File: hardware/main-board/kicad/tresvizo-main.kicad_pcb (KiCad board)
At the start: 4 copper layers, 50 x 76 mm, 143 parts, among them J101 PANEL_USB, J102 BATTERY, J301 U.FL, J302 UM980_AUX, J401 TF-015, J402 PANEL_UI, J403 OLED, J404 NTC, Q101 AO3400A, Q102 AO3401A, Q103 AO3400A, Q401 AO3401A, Q402 AO3400A, SW201 RESET, SW202 BOOT, U101 USBLC6-2SC6, U102 BQ25798RQMR, U103 MAX17048G+T10, U105 TPS62903RPJR, U106 TPS22919DCKR, U201 ESP32-S3-MINI-1-N4R2, U301 UM980, U302 TPS22945DCKR, U401 BMI088

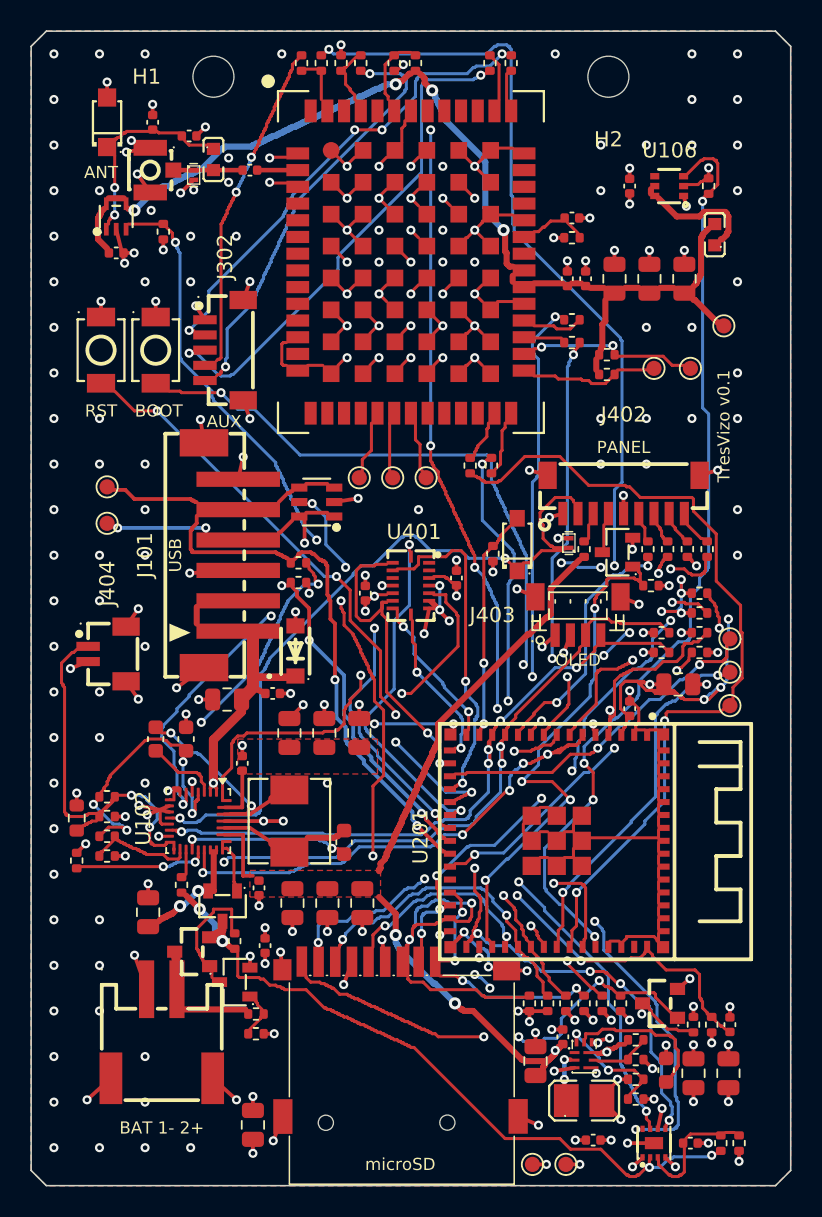
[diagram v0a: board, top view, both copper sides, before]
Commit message: Placa principal v0.2: UM980 y BMI088 por cable, conectores hacia cantos o zonas libres, placa panel-usb y un solo panel para JLCPCB
- 46 x 64 mm, 4 capas. El UM980 queda en su carrier BDLX por J301 (GH 8) con 5 V conmutable
  (TPS63070, GPIO45) y el BMI088 vuelve a la tapa por I2C en un segundo bus (J405, GH 7).
- Todos los conectores de cable son GH o SH de 8 pines o menos (kit del propietario), salvo la
  batería (PH 2). Cada uno apunta a un canto o a una zona libre con sitio para la clavija
  enchufada y su cable: áreas de regla clavija_* en el DRC y kicad/plugs.json para el CAD.
- La placa sube 2.5 mm en el tubo (z 23.5-87.5) para que las clavijas del canto inferior tengan
  7.6 mm hasta la base; rieles propuestos en z 39-90 y agujeros nuevos. Comprobada en FreeCAD
  contra V2.2 con modelos 3D y clavijas: sin choques.
- Cargador según el ejemplo de TI: bootstrap junto a sus pines (0.9 y 1.6 mm), salida en abanico
  de la fila inferior y potencia solo por capas externas.
- Placa panel-usb (USB-C a ras de la tapa del panel, GH 8 a J101) y panel de las dos placas con un
  BOM y un CPL (panelize.py, 82.8 x 78 mm).
- Serigrafía sin solapes (silk_clean.py) y logotipo de TresVizo con www.tresvizo.com.
- ERC 0; DRC con 0 errores, 0 avisos, 0 sin conectar y 0 diferencias de paridad en las dos
  placas y el panel. Costo estimado de montaje y piezas: 211 USD por 5 juegos en un panel, sin
  el PCB desnudo.
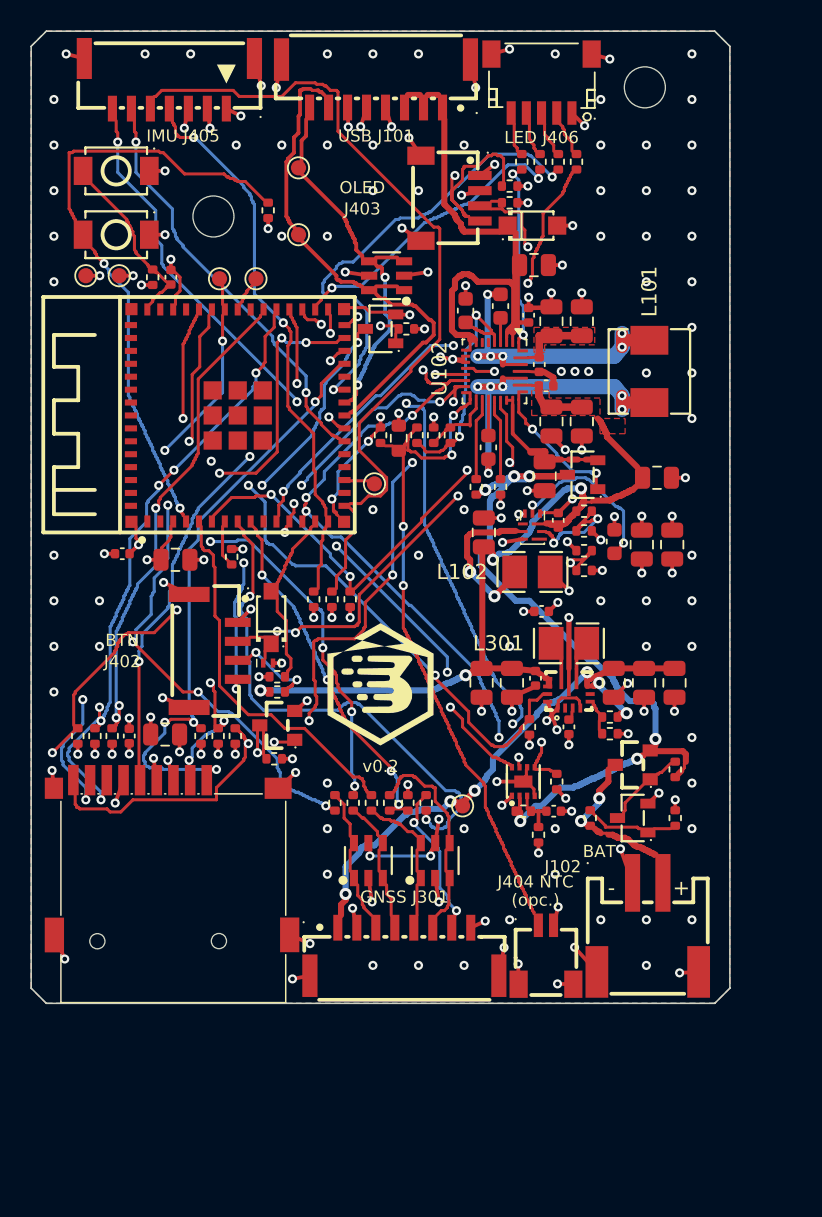
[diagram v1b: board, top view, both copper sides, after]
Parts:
- removed C121, C308, C403, C404: 100nF, Capacitor_SMD:C_0402_1005Metric
- removed C122: 1uF, Capacitor_SMD:C_0402_1005Metric
- removed C309, C310: 100pF, Capacitor_SMD:C_0402_1005Metric
- removed D301: SMF5.0A, tresvizo_lcsc:SOD-123FL_L2.7-W1.8-LS3.8-RD
- removed D302: PESD5V0F1BL, tresvizo_lcsc:SOD-882_L1.0-W0.6-BI
- removed FB101: BLM18PG121SN1D, tresvizo_lcsc:L0603
- removed J302: UM980_AUX, tresvizo_lcsc:CONN-SMD_5P-P1.00_BM05B-SRSS-TB
- removed R120, R122: 100k, Resistor_SMD:R_0402_1005Metric
- removed R121: 22k, Resistor_SMD:R_0402_1005Metric
- removed R310, R311, R313: 100, Resistor_SMD:R_0402_1005Metric
- removed R312: 10k, Resistor_SMD:R_0402_1005Metric
- removed R314, R315, R316: 1k, Resistor_SMD:R_0402_1005Metric
- removed TP302: BIF2, TestPoint:TestPoint_Pad_D1.0mm
- removed TP303: PVT, TestPoint:TestPoint_Pad_D1.0mm
- removed TP304: RTK, TestPoint:TestPoint_Pad_D1.0mm
- removed TP305: ERR, TestPoint:TestPoint_Pad_D1.0mm
- removed TP306: 3V3_GNSS, TestPoint:TestPoint_Pad_D1.0mm
- removed U106: TPS22919DCKR, tresvizo_lcsc:SC-70-6_L2.2-W1.3-P0.65-LS2.1-BR
- removed U401: BMI088, tresvizo_lcsc:LGA-16_L4.5-W3.0-P0.50-BL
- added J405: IMU, tresvizo_lcsc:CONN-SMD_SM7B-GHS-TB-LF-SN, F.Cu at (109.1, 103.5)
- added J406: LEDS, tresvizo_lcsc:CONN-SMD_SM05B-SRSS-TB-LF-SN, F.Cu at (133.6, 103.5)
- added R414: 4.7k, Resistor_SMD:R_0402_1005Metric, F.Cu at (118.6, 137.4)
- added R415: 4.7k, Resistor_SMD:R_0402_1005Metric, F.Cu at (119.8, 137.4)
- added U303: USBLC6-2SC6, tresvizo_lcsc:SOT-23-6_L2.9-W1.6-P0.95-LS2.8-BL, F.Cu at (126.6, 154.6)
- C106, C107: value 10uF -> 22uF
- C108, C112, C116, C303: value 10uF -> 100nF; footprint Capacitor_SMD:C_0805_2012Metric -> Capacitor_SMD:C_0402_1005Metric
- C109, C113: value 100nF -> 22uF; footprint Capacitor_SMD:C_0402_1005Metric -> Capacitor_SMD:C_0805_2012Metric
- C111, C301, C302: value 22uF -> 10uF
- C114, C120: value 22uF -> 100nF; footprint Capacitor_SMD:C_0805_2012Metric -> Capacitor_SMD:C_0402_1005Metric
- C115: value 100nF -> 10uF; footprint Capacitor_SMD:C_0402_1005Metric -> Capacitor_SMD:C_0805_2012Metric
- C117: value 100nF -> 47nF; footprint Capacitor_SMD:C_0402_1005Metric -> Capacitor_SMD:C_0603_1608Metric
- C118: value 47nF -> 22uF; footprint Capacitor_SMD:C_0603_1608Metric -> Capacitor_SMD:C_0805_2012Metric
- C305: value 100pF -> 22uF; footprint Capacitor_SMD:C_0402_1005Metric -> Capacitor_SMD:C_0805_2012Metric
- C306, C307: value 1uF -> 22uF; footprint Capacitor_SMD:C_0402_1005Metric -> Capacitor_SMD:C_0805_2012Metric
- D101: value SMF20A -> SMF15A; footprint tresvizo_lcsc:SOD-123F_L2.8-W1.8-LS3.7-RD -> tresvizo_lcsc:SOD-123FL_L2.7-W1.8-LS3.8-RD
- J101: footprint tresvizo_lcsc:CONN-SMD_6P-P2.00_B6B-PH-SM4-TB-LF-SN -> tresvizo_lcsc:CONN-SMD_8P-P1.25_XUNPU-WAFER-GH1.25-8PWB
- J301: value U.FL -> GNSS; footprint tresvizo_lcsc:IPEX-SMD_BWIPX-1-001E -> tresvizo_lcsc:CONN-SMD_8P-P1.25_XUNPU-WAFER-GH1.25-8PWB
- J402: value PANEL_UI -> BOTON; footprint tresvizo_lcsc:CONN-SMD_9P-P1.00_BM09B-SRSS-TB -> tresvizo_lcsc:CONN-SMD_4P-P1.25_SM04B-GHS-TB-LF-SN
- J403: footprint tresvizo_lcsc:CONN-SMD_BM04B-SRSS-TB -> tresvizo_lcsc:CONN-SMD_4P-P1.00_SM04B-SRSS-TB-LF-SN
- J404: footprint tresvizo_lcsc:CONN-TH_BM02B-SRSS-TB-LF-SN -> tresvizo_lcsc:CONN-SMD_2P-P1.00_SM02B-SRSS-TB-LF-SN
- L301: value 68nH -> 1uH; footprint tresvizo_lcsc:L0603 -> tresvizo_lcsc:L2520
- R101, R117: value 0 -> 10k
- R102: value 0 -> 22k
- R103: value 10k -> 4.7k
- R104: value 22k -> 5.1k
- R105: value 4.7k -> 30k; footprint Resistor_SMD:R_0402_1005Metric -> Resistor_SMD:R_0603_1608Metric
- R106: value 5.1k -> 10k
- R107: value 30k -> 100; footprint Resistor_SMD:R_0603_1608Metric -> Resistor_SMD:R_0402_1005Metric
- R109, R307, R309: value 100 -> 1k
- R110: value 10k -> 1M
- R111, R308: value 1k -> 100k
- R113: value 100k -> 0
- R114: value 1M -> 10k
- R116, R119: value 10k -> 22k
- R118: value 22k -> 100k
- R301: value 0 -> 100k
- R302: value 10k -> 5.1k
- R303, R304: value 10k -> 1k
- R305: value 100k -> 100
- R306: value 1k -> 100
- TP301: value BIF1 -> 5V_GNSS
- U301: value UM980 -> TPS63070RNMR; footprint tresvizo:UM980 -> tresvizo_lcsc:VQFN-15_L3.0-W2.5-P0.50-BL
- U302: value TPS22945DCKR -> USBLC6-2SC6; footprint tresvizo_lcsc:SC-70-5_L2.1-W1.3-P0.65-LS2.1-BL -> tresvizo_lcsc:SOT-23-6_L2.9-W1.6-P0.95-LS2.8-BL
- moved TP201 65.5 mm to (103.6, 116.1)
- moved TP202 65.5 mm to (105.8, 116.1)
- moved R201 61.4 mm to (108.0, 116.2)
- moved C203 61.4 mm to (109.2, 116.2)
- moved J301 53.9 mm to (124.6, 160.6), turned to 0 degrees
- moved R109 52.6 mm to (132.3, 108.6)
- moved R305 48.7 mm to (121.2, 150.8)
- moved C307 46.4 mm to (142.3, 142.9), turned to -90 degrees
- moved U302 45.5 mm to (122.2, 154.6)
- moved R302 44.9 mm to (138.1, 145.2), turned to 180 degrees
- moved TP205 43.8 mm to (112.4, 116.3)
- moved C115 42.4 mm to (129.8, 133.0), turned to 90 degrees
- moved R117 41.6 mm to (136.4, 132.9), turned to 0 degrees
- moved TP204 40.5 mm to (114.8, 116.3)
- moved R202 39.7 mm to (115.6, 111.8), turned to 90 degrees
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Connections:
- net /microSD, IMU y panel/BTN_LED_A renamed /microSD, IMU por conector y panel/BTN_LED_A
- net /microSD, IMU y panel/BTN_LED_K renamed /microSD, IMU por conector y panel/BTN_LED_K
- net /microSD, IMU y panel/SD_CD_N renamed /microSD, IMU por conector y panel/SD_CD_N
- C109 pad 1: /Alimentación, carga y batería/PMID -> VSYS
- C113 pad 1: VSYS -> /Alimentación, carga y batería/VBAT_CHG
- C114 pad 1: /Alimentación, carga y batería/VBAT_CHG -> /Alimentación, carga y batería/FG_VDD
- C115 pad 1: /Alimentación, carga y batería/FG_VDD -> VSYS
- C117 pad 1: VSYS -> /Alimentación, carga y batería/BUCK_SS
- C118 pad 1: /Alimentación, carga y batería/BUCK_SS -> +3V3
- C301 pad 1: +3V3_GNSS -> VSYS
- C302 pad 1: +3V3_GNSS -> VSYS
- C303 pad 1: +3V3_GNSS -> VSYS
- C304 pad 1: +3V3_GNSS -> /GNSS: carrier UM980 por conector y su 5 V/GNSS_VAUX
- C305 pad 1: +3V3_GNSS -> /GNSS: carrier UM980 por conector y su 5 V/GNSS_5V
- C306 pad 1: /GNSS UM980 y antena/GNSS_VBCKP -> /GNSS: carrier UM980 por conector y su 5 V/GNSS_5V
- C307 pad 1: +3V3_GNSS -> /GNSS: carrier UM980 por conector y su 5 V/GNSS_5V
- J101 pad 3: GND -> /Alimentación, carga y batería/VBUS
- J101 pad 4: USB_DN -> GND
- J101 pad 5: USB_DP -> GND
- J301 pad 1: /GNSS UM980 y antena/ANT_RF -> /GNSS: carrier UM980 por conector y su 5 V/GNSS_5V
- J301 pad 3: GND -> /GNSS: carrier UM980 por conector y su 5 V/GNSS_RXD2
- L301 pad 1: /GNSS UM980 y antena/ANT_BIAS -> /GNSS: carrier UM980 por conector y su 5 V/GNSS_L1
- L301 pad 2: /GNSS UM980 y antena/ANT_RF -> /GNSS: carrier UM980 por conector y su 5 V/GNSS_L2
- R101 pad 1: USB_DP -> /Alimentación, carga y batería/REGN
- R101 pad 2: /Alimentación, carga y batería/CHG_DP -> /Alimentación, carga y batería/CHG_ILIM
- R102 pad 1: USB_DN -> /Alimentación, carga y batería/CHG_ILIM
- R102 pad 2: /Alimentación, carga y batería/CHG_DN -> GND
- R103 pad 1: /Alimentación, carga y batería/REGN -> /Alimentación, carga y batería/CHG_PROG
- R103 pad 2: /Alimentación, carga y batería/CHG_ILIM -> GND
- R104 pad 1: /Alimentación, carga y batería/CHG_ILIM -> /Alimentación, carga y batería/REGN
- R104 pad 2: GND -> CHG_TS
- R105 pad 1: /Alimentación, carga y batería/CHG_PROG -> CHG_TS
- R106 pad 1: /Alimentación, carga y batería/REGN -> CHG_TS
- R106 pad 2: CHG_TS -> GND
- R107 pad 1: CHG_TS -> /Alimentación, carga y batería/VPACK
- R107 pad 2: GND -> /Alimentación, carga y batería/CHG_BATP
- R108 pad 1: CHG_TS -> +3V3
- R108 pad 2: GND -> CHG_INT_N
- R109 pad 1: /Alimentación, carga y batería/VPACK -> /Alimentación, carga y batería/CHG_STAT
- R109 pad 2: /Alimentación, carga y batería/CHG_BATP -> CHG_LED_K
- R110 pad 1: +3V3 -> /Alimentación, carga y batería/VPACK
- R110 pad 2: CHG_INT_N -> /Alimentación, carga y batería/BATREV_G
- R111 pad 1: /Alimentación, carga y batería/CHG_STAT -> /Alimentación, carga y batería/VBATT_IN
- R111 pad 2: CHG_LED_K -> /Alimentación, carga y batería/BATREV_SENSE
- R112 pad 1: /Alimentación, carga y batería/VPACK -> /Alimentación, carga y batería/BATREV_SENSE
- R112 pad 2: /Alimentación, carga y batería/BATREV_G -> GND
- R113 pad 1: /Alimentación, carga y batería/VBATT_IN -> /Alimentación, carga y batería/VPACK
- R113 pad 2: /Alimentación, carga y batería/BATREV_SENSE -> /Alimentación, carga y batería/FG_VDD
- R114 pad 1: /Alimentación, carga y batería/BATREV_SENSE -> +3V3
- R114 pad 2: GND -> FG_ALRT_N
- R115 pad 1: /Alimentación, carga y batería/VPACK -> +3V3
- R116 pad 1: +3V3 -> VSYS
- R116 pad 2: FG_ALRT_N -> /Alimentación, carga y batería/BUCK_EN
- R117 pad 1: +3V3 -> /Alimentación, carga y batería/BUCK_EN
- R117 pad 2: /Alimentación, carga y batería/FG_VDD -> GND
- R118 pad 1: VSYS -> +3V3
- R118 pad 2: /Alimentación, carga y batería/BUCK_EN -> /Alimentación, carga y batería/BUCK_FB
- R119 pad 1: /Alimentación, carga y batería/BUCK_EN -> /Alimentación, carga y batería/BUCK_FB
- R301 pad 1: +3V3 -> GNSS_PWR_EN
- R301 pad 2: /GNSS UM980 y antena/GNSS_VBCKP -> GND
- R302 pad 1: +3V3_GNSS -> /GNSS: carrier UM980 por conector y su 5 V/GNSS_5V
- R302 pad 2: /GNSS UM980 y antena/GNSS_RESET_N -> /GNSS: carrier UM980 por conector y su 5 V/GNSS_FB
- R303 pad 1: +3V3_GNSS -> /GNSS: carrier UM980 por conector y su 5 V/GNSS_FB
- R303 pad 2: /GNSS UM980 y antena/GNSS_BIF1 -> GND
- R304 pad 1: +3V3_GNSS -> ESP_TX0
- R304 pad 2: /GNSS UM980 y antena/GNSS_BIF2 -> /GNSS: carrier UM980 por conector y su 5 V/GNSS_RXD2
- R305 pad 1: /GNSS UM980 y antena/GNSS_EVENT -> /GNSS: carrier UM980 por conector y su 5 V/GNSS_TXD2
- R305 pad 2: GND -> GNSS_TXD2_MCU
- R306 pad 1: ESP_TX0 -> /GNSS: carrier UM980 por conector y su 5 V/GNSS_PPS
- R306 pad 2: /GNSS UM980 y antena/GNSS_RXD2 -> GNSS_PPS_MCU
- R307 pad 1: /GNSS UM980 y antena/GNSS_TXD2 -> GNSS_EVENT_MCU
- R307 pad 2: GNSS_TXD2_MCU -> /GNSS: carrier UM980 por conector y su 5 V/GNSS_EVENT
- R308 pad 1: ESP_TX1 -> GNSS_EVENT_MCU
- R308 pad 2: /GNSS UM980 y antena/GNSS_RXD3 -> GND
- R309 pad 1: /GNSS UM980 y antena/GNSS_TXD3 -> GNSS_RESET_MCU
- R309 pad 2: GNSS_TXD3_MCU -> /GNSS: carrier UM980 por conector y su 5 V/GNSS_RESET_N
- R409 pad 2: /microSD, IMU y panel/LED_R_K -> /microSD, IMU por conector y panel/LED_R_K
- R410 pad 2: /microSD, IMU y panel/LED_G_K -> /microSD, IMU por conector y panel/LED_G_K
- R411 pad 2: /microSD, IMU y panel/LED_B_K -> /microSD, IMU por conector y panel/LED_B_K
- TP301 pad 1: /GNSS UM980 y antena/GNSS_BIF1 -> /GNSS: carrier UM980 por conector y su 5 V/GNSS_5V
- U102 pad 6: /Alimentación, carga y batería/CHG_DP -> unconnected-(U102-D+-Pad6)
- U102 pad 7: /Alimentación, carga y batería/CHG_DN -> unconnected-(U102-D--Pad7)
- U201 pad 10: ESP_TX1 -> unconnected-(U201-IO6-Pad10)
- U201 pad 15: IMU_MOSI -> IMU_SDA
- U201 pad 16: IMU_SCK -> IMU_SCL
- U201 pad 17: IMU_MISO -> unconnected-(U201-IO13-Pad17)
- U201 pad 19: IMU_CS_ACC_N -> unconnected-(U201-IO15-Pad19)
- U201 pad 20: IMU_CS_GYR_N -> unconnected-(U201-IO16-Pad20)
- U201 pad 37: ANT_FAULT_N -> unconnected-(U201-IO41-Pad37)
- U201 pad 9: GNSS_TXD3_MCU -> GNSS_EVENT_MCU
- U301 pad 10: unconnected-(U301-SPIS_CLK-Pad10) -> GND
- U301 pad 11: unconnected-(U301-SPIS_MISO-Pad11) -> /GNSS: carrier UM980 por conector y su 5 V/GNSS_L1
- U301 pad 12: GND -> VSYS
- U301 pad 14: GND -> GNSS_PWR_EN
- U301 pad 15: unconnected-(U301-NC-Pad15) -> GND
- U301 pad 2: /GNSS UM980 y antena/GNSS_ANT_IN -> unconnected-(U301-PG-Pad2)
- U301 pad 3: GND -> /GNSS: carrier UM980 por conector y su 5 V/GNSS_VAUX
- U301 pad 4: unconnected-(U301-ANT_DETECT-Pad4) -> GND
- U301 pad 5: unconnected-(U301-ANT_OFF-Pad5) -> /GNSS: carrier UM980 por conector y su 5 V/GNSS_FB
- U301 pad 7: unconnected-(U301-VCC_RF-Pad7) -> /GNSS: carrier UM980 por conector y su 5 V/GNSS_5V
- U301 pad 9: unconnected-(U301-SPIS_MOSI-Pad9) -> /GNSS: carrier UM980 por conector y su 5 V/GNSS_L2
- U302 pad 1: /GNSS UM980 y antena/ANT_BIAS -> /GNSS: carrier UM980 por conector y su 5 V/GNSS_RXD2
- U302 pad 3: ANT_FAULT_N -> /GNSS: carrier UM980 por conector y su 5 V/GNSS_TXD2
- U302 pad 4: +3V3_GNSS -> /GNSS: carrier UM980 por conector y su 5 V/GNSS_TXD2
- U302 pad 5: +3V3_GNSS -> +3V3
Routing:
- net GND: track 200.3 -> 131.5 mm, vias 223 -> 167
- net ANT_FAULT_N: track 63.3 -> 0.00 mm, vias 5 -> 0
- net +3V3_GNSS: track 57.9 -> 0.00 mm, vias 4 -> 0
- net +3V3: track 96.1 -> 39.6 mm, vias 44 -> 36
- net /ESP32-S3/ESP_EN: track 64.2 -> 9.60 mm, vias 5 -> 0
- net IMU_SCL: track 0.00 -> 53.8 mm
- net GNSS_PPS_MCU: track 62.8 -> 24.1 mm, vias 3 -> 0
- net /GNSS: carrier UM980 por conector y su 5 V/GNSS_5V: track 0.00 -> 36.3 mm, vias 0 -> 6
- net FG_ALRT_N: track 73.8 -> 38.3 mm, vias 6 -> 4
- net IMU_SDA: track 0.00 -> 35.3 mm, vias 0 -> 2
- net /GNSS UM980 y antena/AUX_RXD1: track 32.6 -> 0.00 mm, vias 2 -> 0
- net /Alimentación, carga y batería/CHG_STAT: track 42.6 -> 11.6 mm, vias 4 -> 2
- net /GNSS UM980 y antena/AUX_TXD1: track 30.7 -> 0.00 mm, vias 4 -> 0
- net ESP_TX1: track 29.1 -> 0.00 mm, vias 3 -> 0
- net /GNSS UM980 y antena/AUX_EVENT: track 27.7 -> 0.00 mm, vias 2 -> 0
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- added copper zone on In2.Cu, net GND
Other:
- board size 50 x 76 mm -> 46 x 64 mm
- board text added: "(opc.)"
- board text added: "+"
- board text added: "-"
- board text added: "1S: R103=4.7k R117=10k U103=MAX17048"
- board text added: "2026-10 - 4 capas JLC04161H-7628"
- board text added: "2S: R103=8.2k R117=3.9k U103=MAX17049 R113 NC R115 0R"
- board text added: "BAT"
- board text added: "BTN"
- board text added: "GNSS J301"
- board text added: "IMU J405"
- board text added: "J102"
- board text added: "J402"
- board text added: "J403"
- board text added: "J404 NTC"
- board text added: "LED J406"
- board text added: "TresVizo MeridianV - placa principal v0.2"
- board text added: "USB J101"
- board text added: "v0.2"
- board text added: "www.tresvizo.com"
- board text removed: "1S: R105=4.7k R119=10k U103=MAX17048"
- board text removed: "2S: R105=8.2k R119=3.9k U103=MAX17049 R115 NC R117 0R"
- board text removed: "ANT"
- board text removed: "AUX"
- board text removed: "BAT 1- 2+"
- board text removed: "BOOT"
- board text removed: "Ejes (verificar con Bosch fig. 12): X sensor -> derecha, Y sensor -> arriba (antena)"
- board text removed: "IMU BMI088"
- board text removed: "JLCJLCJLCJLC"
- board text removed: "PANEL"
- board text removed: "RST"
- board text removed: "TresVizo MeridianV - placa principal v0.1 (2026-10)"
- board text removed: "TresVizo v0.1"
- board text removed: "USB"
- board text removed: "microSD"

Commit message: Placa principal v0.2: J404 montado con puente JP101, USB-C de la panel-usb más volado, correcciones de la auditoría y logotipo
- J404 (NTC) se monta de fábrica y la NTC queda opcional. Sin ella, R106 (10 kΩ) va a GND por
  JP101, un puente de soldadura cerrado de fábrica, y el cargador ve 25 °C. Para usar la NTC se
  corta JP101 («cortar JP101» en la serigrafía, sobre el puente). R115 baja junto a R113 para
  dejar sitio a esa línea.
- panel-usb: el canto de la lengüeta retrocede 0.8 mm (v = 0.89) y el USB-C sobresale 1.29 mm; su
  cara sigue a ras de la tapa. El cobre queda a 0.41 mm del canto. En el panel la fresa frente al
  USB-C se ensancha a 3 mm (opción cuts de panelize.py) para dejar 1.71 mm hasta el marco; el
  panel pasa a 82.8 x 79 mm.
- Auditoría: VBUS de J101 al cargador con pistas de 0.8 y 1.0 mm, etiquetas de la batería y del
  NTC separadas, planos internos con 0.12 mm de margen y, en el README, medir el pin 1 de la
  carrier antes de enchufar el arnés y la ranura propuesta en la base bajo J102.
- Logotipo: las piezas con huecos se parten en tiras, porque KiCad deformaba al guardar los
  contornos fracturados (el distintivo de la cara de componentes salía mal).
- ERC 0; DRC con 0 errores, 0 avisos, 0 sin conectar y 0 diferencias de paridad en las dos placas
  y el panel. Comprobación en FreeCAD contra V2.2 sin choques nuevos. Costo estimado de montaje y
  piezas: 213.60 USD por 5 juegos en un panel (J404 suma 2.22 USD), sin el PCB desnudo.
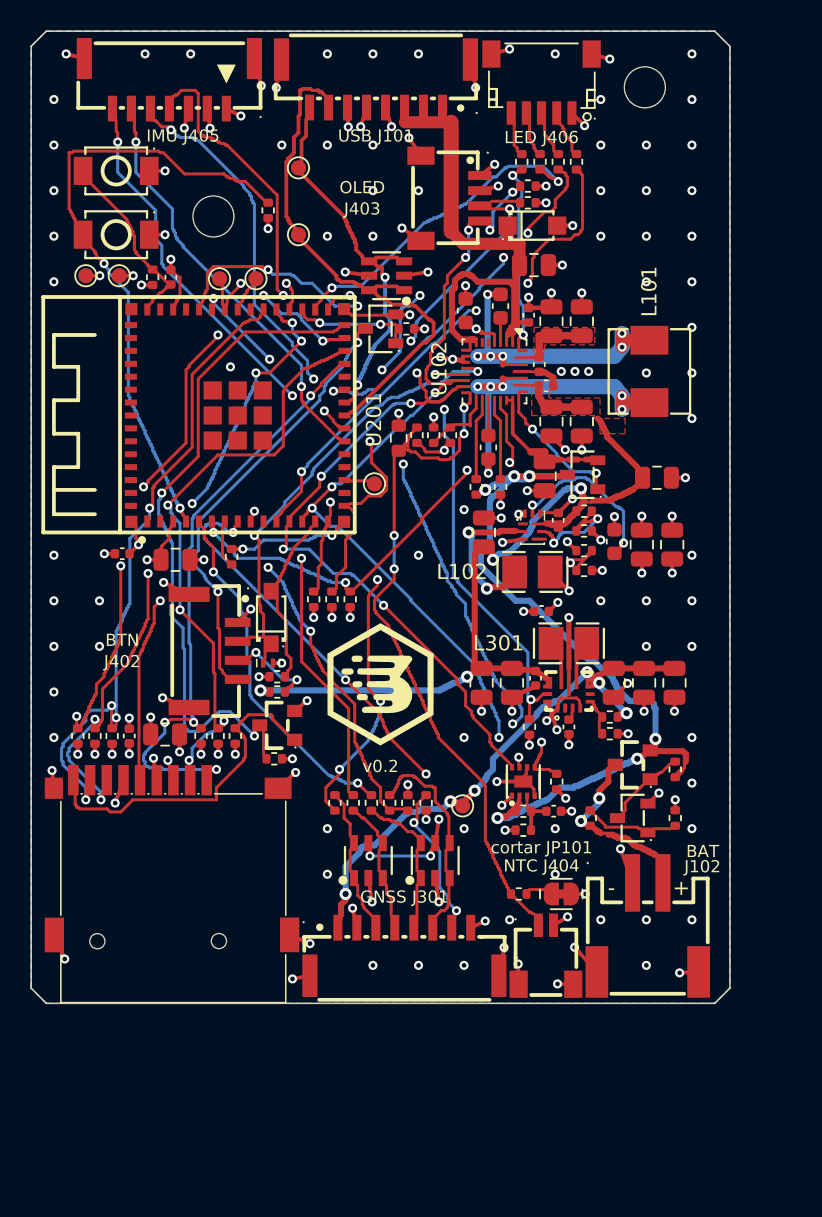
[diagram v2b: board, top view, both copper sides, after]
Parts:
- added JP101: NTC_CORTAR, tresvizo_lcsc:SolderJumper-2_P1.3mm_Bridged_RoundedPad1.0x1.5mm, F.Cu at (134.9, 156.8)
- moved R106 31.5 mm to (132.1, 156.8), turned to 0 degrees
- moved R204 1.20 mm to (132.7, 111.3)
- moved R205 1.20 mm to (132.7, 110.2)
- moved R115 1.04 mm to (132.4, 152.6), turned to 0 degrees
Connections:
- R106 pad 2: GND -> /Alimentación, carga y batería/CHG_TS_FIJA
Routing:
- net IMU_SCL: track 53.8 -> 40.3 mm, vias 0 -> 3
- net I2C_SCL: track 67.7 -> 55.8 mm, vias 7 -> 9
- net LED_G: track 30.3 -> 23.5 mm, vias 2 -> 3
- net FG_ALRT_N: track 38.3 -> 45.0 mm, vias 4 -> 6
- net GNSS_RESET_MCU: track 33.7 -> 28.4 mm, vias 2 -> 4
- net SD_D3: track 33.7 -> 37.9 mm
- net I2C_SDA: track 64.5 -> 60.4 mm, vias 9 -> 7
- net SD_CLK: track 34.2 -> 37.7 mm, vias 3 -> 2
- net GNSS_PWR_EN: track 44.6 -> 47.9 mm, vias 3 -> 4
- net /Alimentación, carga y batería/VBUS: track 34.0 -> 37.3 mm
- net IMU_SDA: track 35.3 -> 38.2 mm
- net ESP_TX0: track 44.1 -> 46.9 mm, vias 6 -> 4
- net /Alimentación, carga y batería/VPACK: track 50.6 -> 53.3 mm
- net LED_B: track 19.3 -> 21.3 mm
- net BTN_N: track 30.7 -> 28.8 mm, vias 4 -> 2
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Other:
- board text added: "NTC J404"
- board text added: "cortar JP101"
- board text removed: "(opc.)"
- board text removed: "J404 NTC"

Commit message: Placa principal v0.2: techo de entrada del USB a ~1.45 A (R102 22k -> 8.2k)
Revisión del propietario: con ILIM en 10k/22k el cargador podía pedir ~2.9 A a cualquier puerto,
sin detectar cuánto da. Con 10k/8.2k desde REGN (4.6-5.0 V) el techo queda en 1.34-1.56 A, que
alcanza para cargar 1S a 1 A con el equipo encendido. La variante 2S vuelve a 22k (~2.9 A).
Solo cambia el valor de R102 (C25924): pistas y gerbers de cobre iguales; ERC 0, DRC 0 en la
placa y en el panel, paridad 0.

README: queda para v0.3 la detección por CC del USB-C y el par diferencial D+/D-, que pide
invertir los pines 7/8 de J101 y J502. En Full Speed la diferencia de largo actual (9 mm, unos
60 ps) no afecta.
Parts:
- R102: value 22k -> 8.2k
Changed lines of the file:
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@@
 			)
 		)
-		(property "Value" "22k"
+		(property "Value" "8.2k"
 			(at 0 1.17 90)
 			(layer "F.Fab")
@@
 			)
 		)
-		(property "MPN" "0402WGF2202TCE"
+		(property "MPN" "0402WGF8201TCE"
 			(at 0 0 90)
 			(layer "F.Fab")
@@
 			)
 		)
-		(property "LCSC" "C25768"
+		(property "LCSC" "C25924"
 			(at 0 0 90)
 			(layer "F.Fab")
